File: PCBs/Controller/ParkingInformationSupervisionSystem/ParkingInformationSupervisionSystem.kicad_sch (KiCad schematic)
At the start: 12 parts, among them J1 08B0-1X1T-03-F, J2 Conn_01x04_Pin, J3 Conn_01x06_Pin, U1 MCU-PIC18F67J60-I_PT_TQFP64_

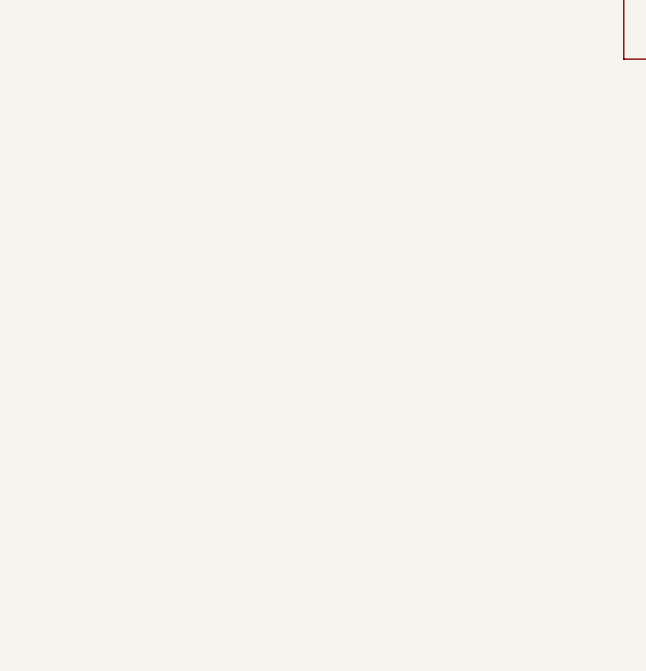
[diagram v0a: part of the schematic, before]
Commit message: Added MOSFET LED drivers to schematic
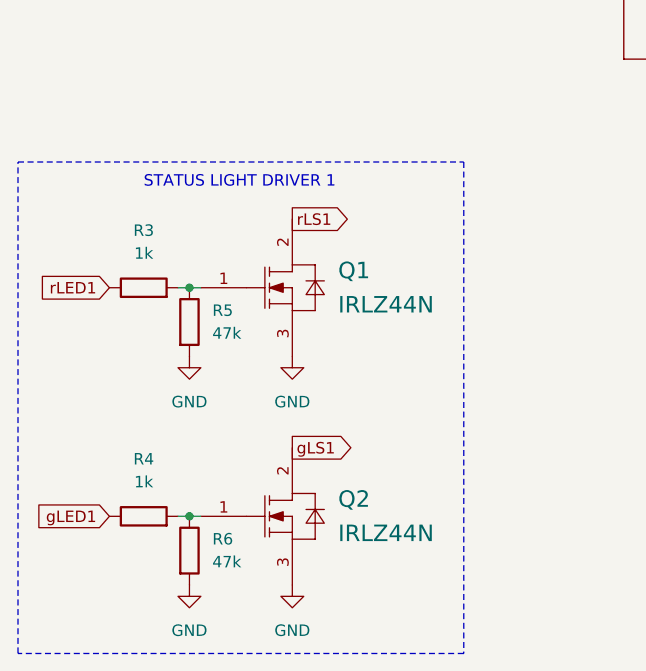
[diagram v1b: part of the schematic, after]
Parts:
- added Q1, Q2: IRLZ44N, IFX-PG-TO220-3-904-1:IFX-PG-TO220-3-904-1, symbol IRLZ44N:IRLZ44N
- added R3, R4: 1k, symbol Device:R
- added R5, R6: 47k, symbol Device:R
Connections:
- net GND: now also Q1.3 (SOURCE), Q2.3 (SOURCE), R5.2, R6.2
- net gLED1: now also R4.1
- net rLED1: now also R3.1
- new net: Q2.1 (GATE), R4.2, R6.1
- new net: Q1.1 (GATE), R3.2, R5.1
- new net gLS1: Q2.2 (DRAIN)
- new net rLS1: Q1.2 (DRAIN)
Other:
- note added: "STATUS LIGHT DRIVER 1"

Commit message: Changes over break, might need to revert things. Probably includes broken vscode stuff.
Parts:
- added R7, R8: 180, symbol Device:R
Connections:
- net GND: now also R7.2, R8.1
- net at J1.7: now also R7.1
- net at J1.9: now also R8.2

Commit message: Started schematic changes for uc transition
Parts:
- added C5: 100n, Capacitor_THT:C_Disc_D10.5mm_W5.0mm_P5.00mm, symbol Device:C
- added U2: STM32F446RET6, STM32F446RET6:QFP50P1200X1200X160-64N, symbol STM32F446RET6:STM32F446RET6
- added U3: W5500, W5500:QFP50P900X900X160-48N, symbol W5500:W5500
- C1, C2, C3, C4: footprint (none) -> Capacitor_THT:C_Disc_D10.5mm_W5.0mm_P5.00mm
- J2: footprint (none) -> Connector_PinSocket_2.54mm:PinSocket_1x04_P2.54mm_Vertical
- J3: footprint (none) -> Connector_PinSocket_2.54mm:PinSocket_1x06_P2.54mm_Vertical
- R1, R2, R3, R4, R5, R6, R7, R8: footprint (none) -> Resistor_THT:R_Axial_DIN0207_L6.3mm_D2.5mm_P7.62mm_Horizontal
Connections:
- net 3V3: now also C5.1, U2.19 (VDD), U2.32 (VDD__1), U2.48 (VDD__2), U2.64 (VDD__3); no longer U1.26 (VDD), U1.38 (VDD@1), U1.57 (VDD@2)
- net ECHO1: now also U2.8 (PC0/SAI1_MCLK_B/OTG_HS_ULPI_STP/FMC_SDNWE/EVENTOUT)
- net GND: now also C5.2, U2.18 (VSS), U2.31 (VSS__1), U2.47 (VSS__2), U2.63 (VSS__3)
- net TRIG1: now also U2.9 (PC1/SPI3_MOSI/I2S3_SD/SAI1_SD_A/SPI2_MOSI/I2S2_SD/EVENTOUT)
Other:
- moved on the sheet: C1, C2, C3, C4, J1, J3, Q1, Q2, R3, R4, R5, R6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

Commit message: Added STM32CubeMX project, updated more of the code, updated schematic a bit.
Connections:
- net 3V3: now also U3.11 (AVDD__2), U3.15 (AVDD__3), U3.17 (AVDD__4), U3.21 (AVDD__5), U3.28 (VDD), U3.4 (AVDD), U3.8 (AVDD__1)
- net GND: now also U3.14 (AGND__2), U3.16 (AGND__3), U3.19 (AGND__4), U3.29 (GND), U3.3 (AGND), U3.48 (AGND__5), U3.9 (AGND__1)
- net gLED1: now also U2.15 (PA1/TIM2_CH2/TIM5_CH2/USART2_RTS/UART4_RX/QUADSPI_BK1_IO3/SAI2_MCLK_B/EVENTOUT)
- net rLED1: now also U2.14 (PA0-WKUP(PA0)TIM2_CH1/TIM2_ETR/TIM5_CH1/TIM8_ETR/USART2_CTS/UART4_TX/EVENTOUT)

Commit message: Added basic ethernet functionality. Specifically the abilty to get the spot status using http. Also added updated schematic.
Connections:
- net ethCS: now reaches U2.20 (PA4/SPI1_NSS/I2S1_WS/SPI3_NSS/I2S3_WS/USART2_CK/OTG_HS_SOF/DCMI_HSYNC/EVENTOUT)
- net ethCS: now also U3.32 (~{SCSN})
- net ethSCK: now reaches U2.21 (PA5/TIM2_CH1/TIM2_ETR/TIM8_CH1N/SPI1_SCK/I2S1_CK/OTG_HS_ULPI_CK/EVENTOUT)
- net ethSCK: now also U3.33 (SCLK)
- net ethMISO: now reaches U2.22 (PA6/TIM1_BKIN/TIM3_CH1/TIM8_BKIN/SPI1_MISO/I2S2_MCK/TIM13_CH1/DCMI_PIXCLK/EVENTOUT)
- net ethMISO: now also U3.34 (MISO)
- net ethMOSI: now reaches U2.23 (PA7/TIM1_CH1N/TIM3_CH2/TIM8_CH1N/SPI1_MOSI/I2S1_SD/TIM14_CH1/FMC_SDNWE/EVENTOUT)
- net ethMOSI: now also U3.35 (MOSI)
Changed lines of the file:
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@@
+		)
+	)
+	(global_label "ethCS"
+		(shape bidirectional)
+		(at 436.88 106.68 180)
+		(fields_autoplaced yes)
+		(effects
+			(font
+				(size 1.27 1.27)
+			)
+			(justify right)
+		)
+		(property "Intersheetrefs" "${INTERSHEET_REFS}"
+			(at 427.3407 106.68 0)
+			(effects
+				(font
+					(size 1.27 1.27)
+				)
+				(justify right)
+				(hide yes)
+			)
 		)
 	)
@@
 		)
 	)
+	(global_label "ethMISO"
+		(shape bidirectional)
+		(at 39.37 303.53 180)
+		(fields_autoplaced yes)
+		(effects
+			(font
+				(size 1.27 1.27)
+			)
+			(justify right)
+		)
+		(property "Intersheetrefs" "${INTERSHEET_REFS}"
+			(at 27.714 303.53 0)
+			(effects
+				(font
+					(size 1.27 1.27)
+				)
+				(justify right)
+				(hide yes)
+			)
+		)
+	)
 	(global_label "ECHO1"
 		(shape input)
@@
 		)
 	)
+	(global_label "ethMISO"
+		(shape bidirectional)
+		(at 436.88 101.6 180)
+		(fields_autoplaced yes)
+		(effects
+			(font
+				(size 1.27 1.27)
+			)
+			(justify right)
+		)
+		(property "Intersheetrefs" "${INTERSHEET_REFS}"
+			(at 425.224 101.6 0)
+			(effects
+				(font
+					(size 1.27 1.27)
+				)
+				(justify right)
+				(hide yes)
+			)
+		)
+	)
 	(global_label "3V3"
 		(shape input)
@@
 		)
 	)
+	(global_label "ethSCK"
+		(shape bidirectional)
+		(at 436.88 104.14 180)
+		(fields_autoplaced yes)
+		(effects
+			(font
+				(size 1.27 1.27)
+			)
+			(justify right)
+		)
+		(property "Intersheetrefs" "${INTERSHEET_REFS}"
+			(at 426.0707 104.14 0)
+			(effects
+				(font
+					(size 1.27 1.27)
+				)
+				(justify right)
+				(hide yes)
+			)
+		)
+	)
+	(global_label "ethMOSI"
+		(shape bidirectional)
+		(at 39.37 306.07 180)
+		(fields_autoplaced yes)
+		(effects
+			(font
+				(size 1.27 1.27)
+			)
+			(justify right)
+		)
+		(property "Intersheetrefs" "${INTERSHEET_REFS}"
+			(at 27.714 306.07 0)
+			(effects
+				(font
+					(size 1.27 1.27)
+				)
+				(justify right)
+				(hide yes)
+			)
+		)
+	)
 	(global_label "LEDA"
 		(shape output)
@@
 		)
 	)
+	(global_label "ethSCK"
+		(shape bidirectional)
+		(at 39.37 300.99 180)
+		(fields_autoplaced yes)
+		(effects
+			(font
+				(size 1.27 1.27)
+			)
+			(justify right)
+		)
+		(property "Intersheetrefs" "${INTERSHEET_REFS}"
+			(at 28.5607 300.99 0)
+			(effects
+				(font
+					(size 1.27 1.27)
+				)
+				(justify right)
+				(hide yes)
+			)
+		)
+	)
 	(global_label "rLS1"
 		(shape output)
@@
 		)
 	)
+	(global_label "ethCS"
+		(shape bidirectional)
+		(at 39.37 298.45 180)
+		(fields_autoplaced yes)
+		(effects
+			(font
+				(size 1.27 1.27)
+			)
+			(justify right)
+		)
+		(property "Intersheetrefs" "${INTERSHEET_REFS}"
+			(at 29.8307 298.45 0)
+			(effects
+				(font
+					(size 1.27 1.27)
+				)
+				(justify right)
+				(hide yes)
+			)
+		)
+	)
 	(global_label "RST"
 		(shape output)
@@
 				(hide yes)
 			)
+		)
+	)
+	(global_label "ethMOSI"
+		(shape bidirectional)
+		(at 436.88 99.06 180)
+		(fields_autoplaced yes)
+		(effects
+			(font
+				(size 1.27 1.27)
+			)
+			(justify right)
+		)
+		(property "Intersheetrefs" "${INTERSHEET_REFS}"
+			(at 425.224 99.06 0)
+			(effects
+				(font
+					(size 1.27 1.27)
+				)
+				(justify right)
+				(hide yes)
+			)
